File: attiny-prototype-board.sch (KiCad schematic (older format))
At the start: 50 parts, among them J1 Banana, J10 banana, J11 banana, J12 banana, J13 tinyLeft, J14 TRS35, J15 toPoti, J16 toAudio, J17 USART, J18 TRS35, J19 toPoti, J2 Banana, J20 GND, J21 toBtn, J22 toPoti, J23 VCC, J25 I2C, J3 Banana, J4 Banana, J5 tinyRight, J6 toPoti, J7 tinyRight, J8 tinyRight, J9 banana, SW1 SW_SPDT, SW2 Switch UPDI, SW3 SW_Push, SW4 SW_SPDT, SW5 SW_Push, SW6 SW_SPDT, SW7 SW_SPDT, U1 FTDI-Adapter, U2 ATtinyXX14-SS

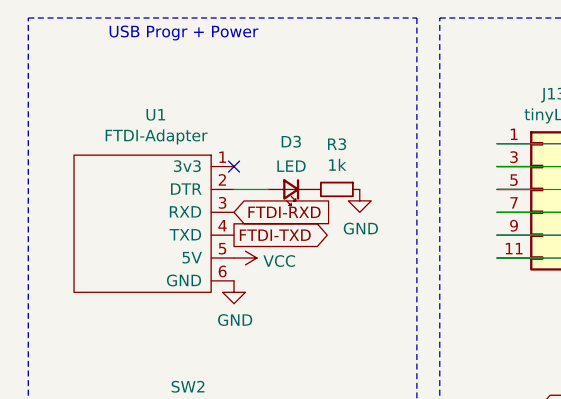
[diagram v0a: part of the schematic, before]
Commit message: fix lib path
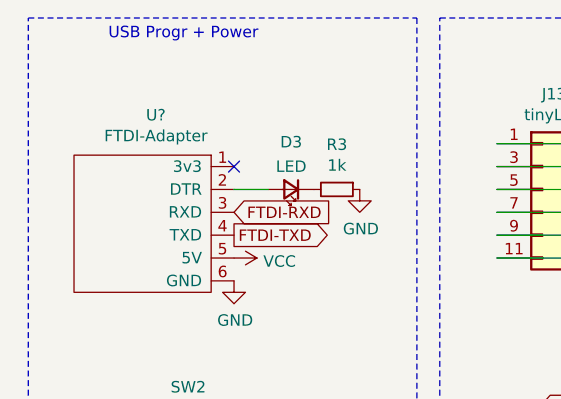
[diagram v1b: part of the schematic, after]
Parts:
- removed U1: FTDI-Adapter, ftdi:FTDI, symbol ftdi:FTDI-Adapter
- added U?: FTDI-Adapter, symbol ftdi:FTDI-Adapter
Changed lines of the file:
@@
 	7900 2100 7400 2100
 $Comp
-L ftdi:FTDI-Adapter U1
-U 1 1 657DE8F5
+L ftdi:FTDI-Adapter U?
+U 1 1 657DF270
 P 1150 1500
-F 0 "U1" H 1208 1975 50  0000 C CNN
+F 0 "U?" H 1208 1975 50  0000 C CNN
 F 1 "FTDI-Adapter" H 1208 1884 50  0000 C CNN
-F 2 "ftdi:FTDI" H 1350 1500 50  0001 C CNN
+F 2 "" H 1350 1500 50  0001 C CNN
 F 3 "" H 1350 1500 50  0001 C CNN
 	1    1150 1500

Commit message: v2.1 some improvements
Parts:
- removed SW3, SW5: SW_Push, ftdi:PushBtn6x6, symbol Switch:SW_Push
- removed SW6, SW7: SW_SPDT, ftdi:Switch_SPDT_1P2T, symbol Switch:SW_SPDT
- added SW10, SW9: SW_Push_DPDT, ftdi:PushBtn6x6, symbol Switch:SW_Push_DPDT
- added SW3, SW8: 2x Switch, ftdi:Switch_SPDT_2P2T, symbol AudioChannel-cache:Switch_SW_Push_DPDT
- R5, R6: value 10k -> 1.5k
- U1: renamed from U?; footprint (none) -> AudioChannel:FTDI
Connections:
- wire segments 162 -> 177
- no-connect marks 1 -> 3
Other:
- moved on the sheet: J21, J25, J8, R5, R6

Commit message: v2.1 move USART
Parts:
- R3, R4: footprint Resistor_THT:R_Axial_DIN0204_L3.6mm_D1.6mm_P1.90mm_Vertical -> Resistor_THT:R_Axial_DIN0207_L6.3mm_D2.5mm_P10.16mm_Horizontal
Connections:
- net GND: now also D1.1 (K), D2.1 (K), D5.1 (K), D6.1 (K); no longer R1.1, R2.1, R7.1, R8.1
- net at R7.2: now also J6.3 (Pin_3), J6.4 (Pin_4); no longer D2.1 (K)
- net at R2.2: now also J6.5 (Pin_5), J6.6 (Pin_6); no longer D5.1 (K)
- net at R1.2: now also J6.1 (Pin_1), J6.2 (Pin_2); no longer D1.1 (K)
- net at J6.7 (Pin_7), J6.8 (Pin_8): now also R8.2; no longer D6.2 (A)
- new net: D2.2 (A), R7.1
- new net: D5.2 (A), R2.1
- new net: D1.2 (A), R1.1
- new net: D6.2 (A), R8.1
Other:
- moved on the sheet: D1, D2, D5, D6, R1, R2, R7, R8
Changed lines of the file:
@@
 F 0 "R4" V 1550 3000 50  0000 C CNN
 F 1 "1k" V 1750 3000 50  0000 C CNN
-F 2 "Resistor_THT:R_Axial_DIN0204_L3.6mm_D1.6mm_P1.90mm_Vertical" H 1650 3000 50  0001 C CNN
+F 2 "Resistor_THT:R_Axial_DIN0207_L6.3mm_D2.5mm_P10.16mm_Horizontal" H 1650 3000 50  0001 C CNN
 F 3 "~" H 1650 3000 50  0001 C CNN
 	1    1650 3000
@@
 L Device:LED_Small D2
 U 1 1 655F2501
-P 6350 1100
-F 0 "D2" H 6450 1050 50  0000 C CNN
-F 1 "LED" H 6250 1050 50  0000 C CNN
-F 2 "LED_THT:LED_D3.0mm" V 6350 1100 50  0001 C CNN
-F 3 "~" V 6350 1100 50  0001 C CNN
-	1    6350 1100
+P 6650 1100
+F 0 "D2" H 6750 1050 50  0000 C CNN
+F 1 "LED" H 6550 1050 50  0000 C CNN
+F 2 "LED_THT:LED_D3.0mm" V 6650 1100 50  0001 C CNN
+F 3 "~" V 6650 1100 50  0001 C CNN
+	1    6650 1100
 	-1   0    0    1
 $EndComp
@@
 L Device:R_Small R2
 U 1 1 655F2507
-P 6650 1200
-F 0 "R2" V 6600 1350 50  0000 C CNN
-F 1 "1k" V 6650 1200 50  0000 C CNN
-F 2 "Resistor_THT:R_Axial_DIN0204_L3.6mm_D1.6mm_P1.90mm_Vertical" H 6650 1200 50  0001 C CNN
-F 3 "~" H 6650 1200 50  0001 C CNN
-	1    6650 1200
+P 6350 1200
+F 0 "R2" V 6300 1100 50  0000 C CNN
+F 1 "1k" V 6350 1200 50  0000 C CNN
+F 2 "Resistor_THT:R_Axial_DIN0204_L3.6mm_D1.6mm_P1.90mm_Vertical" H 6350 1200 50  0001 C CNN
+F 3 "~" H 6350 1200 50  0001 C CNN
+	1    6350 1200
 	0    1    1    0
 $EndComp
@@
 L Device:LED_Small D1
 U 1 1 655F4894
-P 6350 1000
-F 0 "D1" H 6450 950 50  0000 C CNN
-F 1 "LED" H 6250 950 50  0000 C CNN
-F 2 "LED_THT:LED_D3.0mm" V 6350 1000 50  0001 C CNN
-F 3 "~" V 6350 1000 50  0001 C CNN
-	1    6350 1000
+P 6650 1000
+F 0 "D1" H 6750 950 50  0000 C CNN
+F 1 "LED" H 6550 950 50  0000 C CNN
+F 2 "LED_THT:LED_D3.0mm" V 6650 1000 50  0001 C CNN
+F 3 "~" V 6650 1000 50  0001 C CNN
+	1    6650 1000
 	-1   0    0    1
 $EndComp
@@
 L Device:R_Small R1
 U 1 1 655F489A
-P 6650 1000
-F 0 "R1" V 6600 1150 50  0000 C CNN
-F 1 "1k" V 6650 1000 50  0000 C CNN
-F 2 "Resistor_THT:R_Axial_DIN0204_L3.6mm_D1.6mm_P1.90mm_Vertical" H 6650 1000 50  0001 C CNN
-F 3 "~" H 6650 1000 50  0001 C CNN
-	1    6650 1000
+P 6350 1000
+F 0 "R1" V 6300 900 50  0000 C CNN
+F 1 "1k" V 6350 1000 50  0000 C CNN
+F 2 "Resistor_THT:R_Axial_DIN0204_L3.6mm_D1.6mm_P1.90mm_Vertical" H 6350 1000 50  0001 C CNN
+F 3 "~" H 6350 1000 50  0001 C CNN
+	1    6350 1000
 	0    1    1    0
 $EndComp
@@
 F 0 "R3" V 1804 1350 50  0000 C CNN
 F 1 "1k" V 1895 1350 50  0000 C CNN
-F 2 "Resistor_THT:R_Axial_DIN0204_L3.6mm_D1.6mm_P1.90mm_Vertical" H 2000 1350 50  0001 C CNN
+F 2 "Resistor_THT:R_Axial_DIN0207_L6.3mm_D2.5mm_P10.16mm_Horizontal" H 2000 1350 50  0001 C CNN
 F 3 "~" H 2000 1350 50  0001 C CNN
 	1    2000 1350
@@
 L Device:LED_Small D5
 U 1 1 65777648
-P 6350 1200
-F 0 "D5" H 6450 1150 50  0000 C CNN
-F 1 "LED" H 6250 1150 50  0000 C CNN
-F 2 "LED_THT:LED_D3.0mm" V 6350 1200 50  0001 C CNN
-F 3 "~" V 6350 1200 50  0001 C CNN
-	1    6350 1200
+P 6650 1200
+F 0 "D5" H 6750 1150 50  0000 C CNN
+F 1 "LED" H 6550 1150 50  0000 C CNN
+F 2 "LED_THT:LED_D3.0mm" V 6650 1200 50  0001 C CNN
+F 3 "~" V 6650 1200 50  0001 C CNN
+	1    6650 1200
 	-1   0    0    1
 $EndComp
@@
 L Device:LED_Small D6
 U 1 1 65777965
-P 6350 1300
-F 0 "D6" H 6450 1250 50  0000 C CNN
-F 1 "LED" H 6250 1250 50  0000 C CNN
-F 2 "LED_THT:LED_D3.0mm" V 6350 1300 50  0001 C CNN
-F 3 "~" V 6350 1300 50  0001 C CNN
-	1    6350 1300
+P 6650 1300
+F 0 "D6" H 6750 1250 50  0000 C CNN
+F 1 "LED" H 6550 1250 50  0000 C CNN
+F 2 "LED_THT:LED_D3.0mm" V 6650 1300 50  0001 C CNN
+F 3 "~" V 6650 1300 50  0001 C CNN
+	1    6650 1300
 	-1   0    0    1
 $EndComp
@@
 L Device:R_Small R7
 U 1 1 65778177
-P 6650 1100
-F 0 "R7" V 6600 1250 50  0000 C CNN
-F 1 "1k" V 6650 1100 50  0000 C CNN
-F 2 "Resistor_THT:R_Axial_DIN0204_L3.6mm_D1.6mm_P1.90mm_Vertical" H 6650 1100 50  0001 C CNN
-F 3 "~" H 6650 1100 50  0001 C CNN
-	1    6650 1100
+P 6350 1100
+F 0 "R7" V 6300 1000 50  0000 C CNN
+F 1 "1k" V 6350 1100 50  0000 C CNN
+F 2 "Resistor_THT:R_Axial_DIN0204_L3.6mm_D1.6mm_P1.90mm_Vertical" H 6350 1100 50  0001 C CNN
+F 3 "~" H 6350 1100 50  0001 C CNN
+	1    6350 1100
 	0    1    1    0
 $EndComp
@@
 L Device:R_Small R8
 U 1 1 657783D2
-P 6650 1300
-F 0 "R8" V 6600 1450 50  0000 C CNN
-F 1 "1k" V 6650 1300 50  0000 C CNN
-F 2 "Resistor_THT:R_Axial_DIN0204_L3.6mm_D1.6mm_P1.90mm_Vertical" H 6650 1300 50  0001 C CNN
-F 3 "~" H 6650 1300 50  0001 C CNN
-	1    6650 1300
-	0    1    1    0
-$EndComp
+P 6350 1300
+F 0 "R8" V 6300 1200 50  0000 C CNN
+F 1 "1k" V 6350 1300 50  0000 C CNN
+F 2 "Resistor_THT:R_Axial_DIN0204_L3.6mm_D1.6mm_P1.90mm_Vertical" H 6350 1300 50  0001 C CNN
+F 3 "~" H 6350 1300 50  0001 C CNN
+	1    6350 1300
+	0    1    1    0
+$EndComp
